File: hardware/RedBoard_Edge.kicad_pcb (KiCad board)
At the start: 2 copper layers, 101.6 x 38.1 mm, 56 parts, among them J1 CONN_025MM, J17 QWIIC_CONNECTORJS-1MM, J2 CONN_03X2SMT, J4 USB_MICRO-B_FEMALE-SMT, J5 CONN_04, J6 CONN_04, Q1 MOSFET_PCH-SI2309DS, Q2 MOSFET-NCH-BSS138, U1 CH340GSMD, U2 V_REG_MIC52053.3V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

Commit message: v02
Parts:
- added 5V1: CONN_04, Connectors:1X04_NO_SILK, F.Cu at (159.5, 83.1)
- added 5V2: CONN_04, Connectors:1X04_NO_SILK, F.Cu at (184.9, 83.1)
- added 5V3: CONN_04, Connectors:1X04_NO_SILK, F.Cu at (172.2, 83.1)
- added 5V4: CONN_04, Connectors:1X04_NO_SILK, F.Cu at (149.4, 83.1)
- added ADC1: CONN_04, Connectors:1X04_NO_SILK, F.Cu at (159.5, 80.5)
- added ADC4: CONN_04, Connectors:1X04_NO_SILK, F.Cu at (149.4, 80.5)
- added GND1: CONN_04, Connectors:1X04_NO_SILK, F.Cu at (159.5, 85.6)
- added GND2: CONN_04, Connectors:1X04_NO_SILK, F.Cu at (184.9, 85.6)
- added GND3: CONN_04, Connectors:1X04_NO_SILK, F.Cu at (172.2, 85.6)
- added GND4: CONN_04, Connectors:1X04_NO_SILK, F.Cu at (149.4, 85.6)
- added J20: POWER_JACKSMD, Connectors:POWER_JACK_SMD_GND, F.Cu at (115.8, 114.0)
- added LOGO1: SFE_LOGO_NAME_FLAME.1_INCH, Aesthetics:SFE_LOGO_NAME_FLAME_.1, B.Cu at (123.4, 95.2)
- added Q3: MOSFET-NCH-BSS138, Silicon-Standard:SOT23-3, F.Cu at (145.0, 81.3)
- added R10: 4.7KOHM-0603-1_10W-1%, Resistors:0603, F.Cu at (144.0, 84.3)
- added R8: 4.7KOHM-0603-1_10W-1%, Resistors:0603, F.Cu at (146.1, 92.8)
- added S1: MOMENTARY-SWITCH-SPST-2-PTH-RT-ANGLE, Switches:SWITCH TACTILE SPST-NO 0.05A 12V, F.Cu at (190.3, 112.3)
- C5: value 47UF-POLAR-EIA3528-10V-10% -> 47UF-POLAR-PANASONIC_D-35V-20%; footprint Capacitors:EIA3528 -> Capacitors:PANASONIC_D
- FD1, FD2, FD3, FD4: footprint Aesthetics:FIDUCIAL-MICRO -> Aesthetics:FIDUCIAL-1X2
- H1, H2: footprint Hardware:STAND-OFF-TIGHT -> Hardware:STAND-OFF
- J17: footprint SparkX:SparkX-1X04_1MM_RA -> Connectors:1X04_1MM_RA
- J5, J6, PWM1, SPI1: footprint Connectors:1X04 -> Connectors:1X04_NO_SILK
- LOGO2: footprint OSHW-LOGO-S -> Aesthetics:OSHW-LOGO-S
- Y2: footprint Clocks:CRYSTAL-SMD-3.2X2.5MM -> Clocks:CRYSTAL-SMD-5X3.2-4PAD
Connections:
- Q1 pad 1: Net-(J20-PadP$4) -> GND
- R4 pad 1: Net-(J20-PadP$4) -> GND
- U4 pad 17: Net-(U4-Pad17) -> /SCK
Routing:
- net 5V: track 218.1 -> 0.00 mm, vias 10 -> 0
- net 3.3V: track 132.3 -> 0.00 mm, vias 5 -> 0
- net /SCK: track 91.2 -> 0.00 mm, vias 2 -> 0
- net VIN: track 67.3 -> 0.00 mm
- net /HI_SDA: track 63.4 -> 0.00 mm, vias 3 -> 0
- net /usb_shield: track 60.5 -> 0.00 mm, vias 2 -> 0
- net /HI_SCL: track 56.8 -> 0.00 mm, vias 3 -> 0
- net /PWM3: track 53.9 -> 0.00 mm, vias 2 -> 0
- net /AD7: track 45.3 -> 0.00 mm, vias 2 -> 0
- net /AD6: track 44.9 -> 0.00 mm, vias 2 -> 0
- net Net-(J20-PadVIN0): track 42.0 -> 0.00 mm
- net Net-(J4-PadD-): track 39.6 -> 0.00 mm, vias 2 -> 0
- net Net-(J4-PadD+): track 38.3 -> 0.00 mm, vias 2 -> 0
- net /RESET: track 37.2 -> 0.00 mm, vias 1 -> 0
- net /MOSI: track 35.4 -> 0.00 mm, vias 2 -> 0
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- removed copper zone on B.Cu, net GND
- removed copper zone on F.Cu, net GND
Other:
- board outline removed
- board text removed: "+"
- board text removed: "-"
- board text removed: "10"
- board text removed: "11"
- board text removed: "12"
- board text removed: "13"
- board text removed: "3"
- board text removed: "3V3"
- board text removed: "5"
- board text removed: "5V"
- board text removed: "6"
- board text removed: "7-15VDC"
- board text removed: "9"
- board text removed: "A0"
- board text removed: "A1"
- board text removed: "A2"
- board text removed: "A3"
- board text removed: "A4"
- board text removed: "A5"
- board text removed: "A6"
- board text removed: "A7"
- board text removed: "ADC"
- board text removed: "Designed by: Nick Poole"
- board text removed: "GND"
- board text removed: "ISP"
- board text removed: "PWM"
- board text removed: "PWR"
- board text removed: "QWIIC"
- board text removed: "RESET"
- board text removed: "ROCKER SWITCH"
- board text removed: "RX"
- board text removed: "RedBoard Edge"
- board text removed: "Revised by: Andy England"
- board text removed: "SHIELD"
- board text removed: "SPI"
- board text removed: "Standoff O.C."
- board text removed: "TX"
- board text removed: "VIN"
- board text removed: "v01"

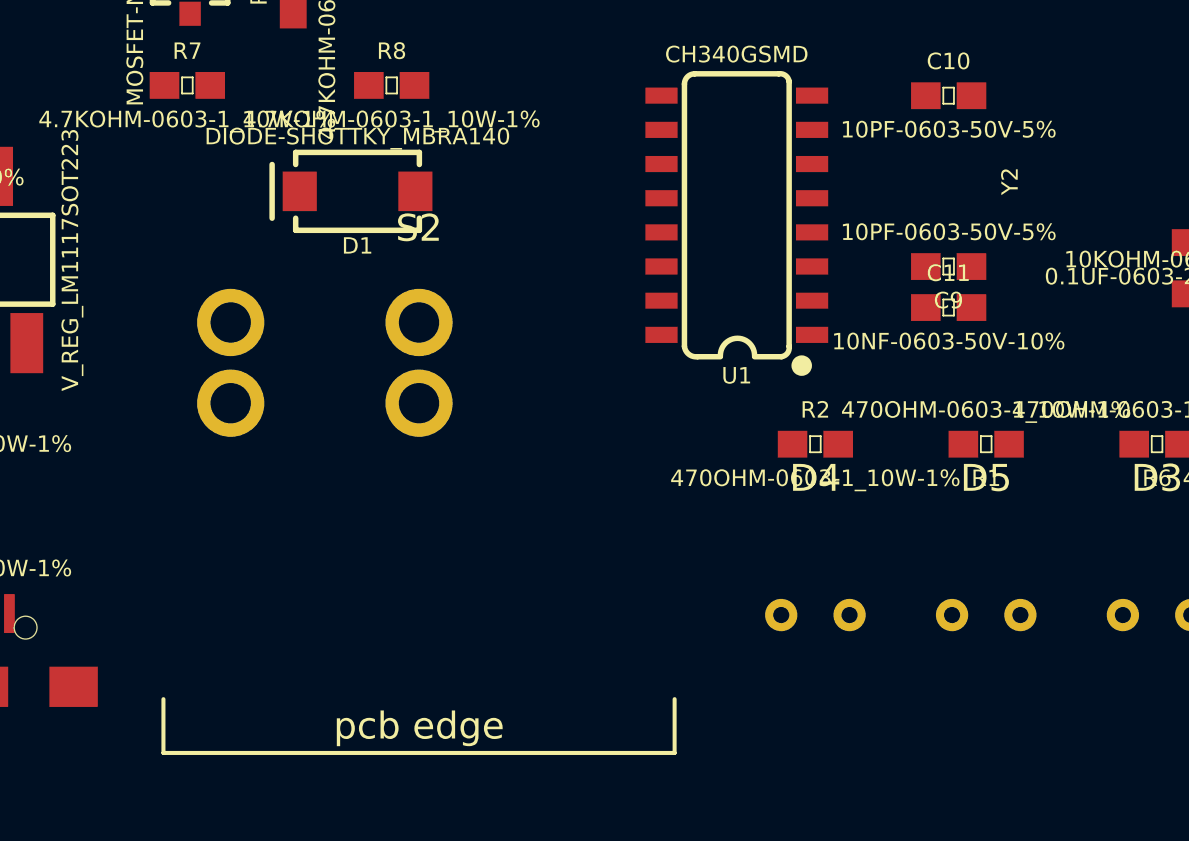
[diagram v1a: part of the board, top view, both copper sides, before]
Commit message: post design review changes, added switch
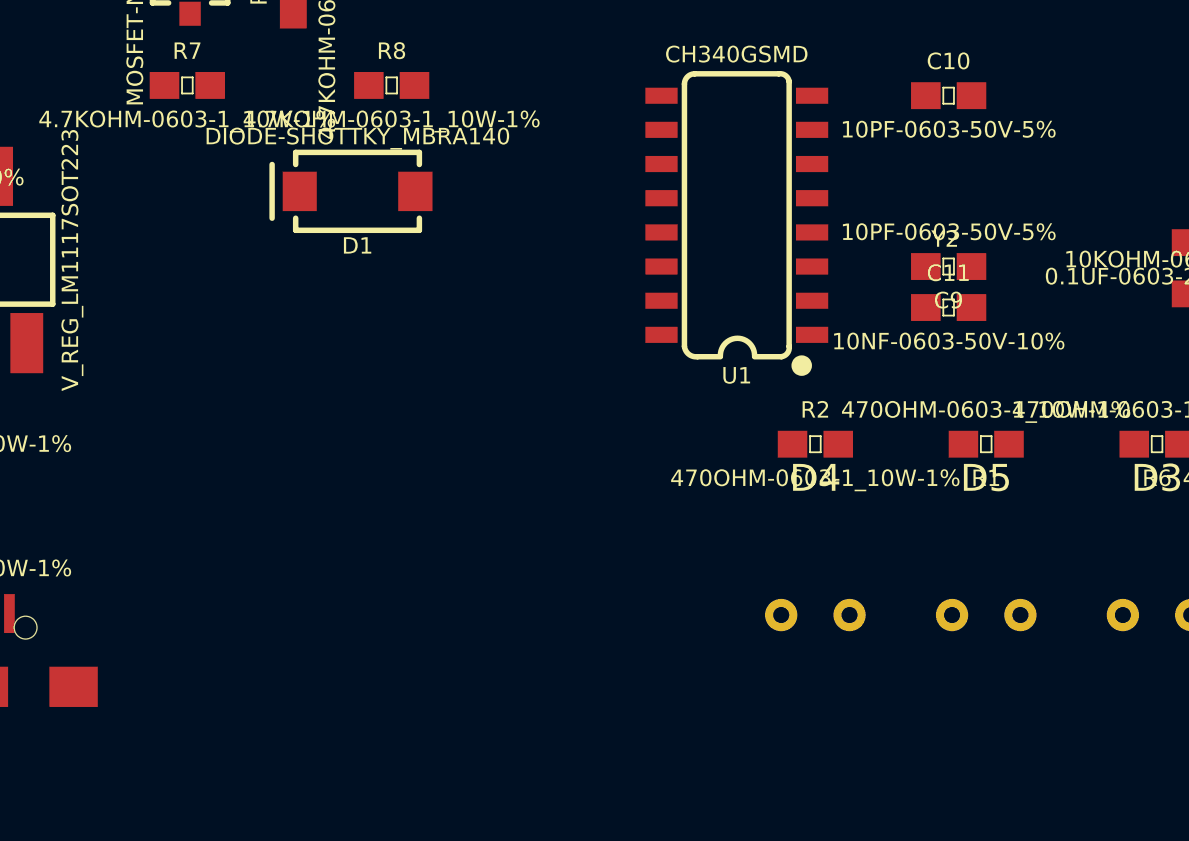
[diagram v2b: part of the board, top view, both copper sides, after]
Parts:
- removed S2: ROCKER_SWITCH-SPST_PTH_RIGHT_ANGLE, Switches:RockerSwitch_RA
- moved Y2 0.18 mm to (166.6, 96.3), turned to 180 degrees
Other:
- net class fat added: clearance 0.1524, trace_width 1.27, via_dia 0.6, via_drill 0.4
